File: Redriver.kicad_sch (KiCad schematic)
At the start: 124 parts, among them U1 DS320PR810NJXR, U2 DS320PR810NJXR

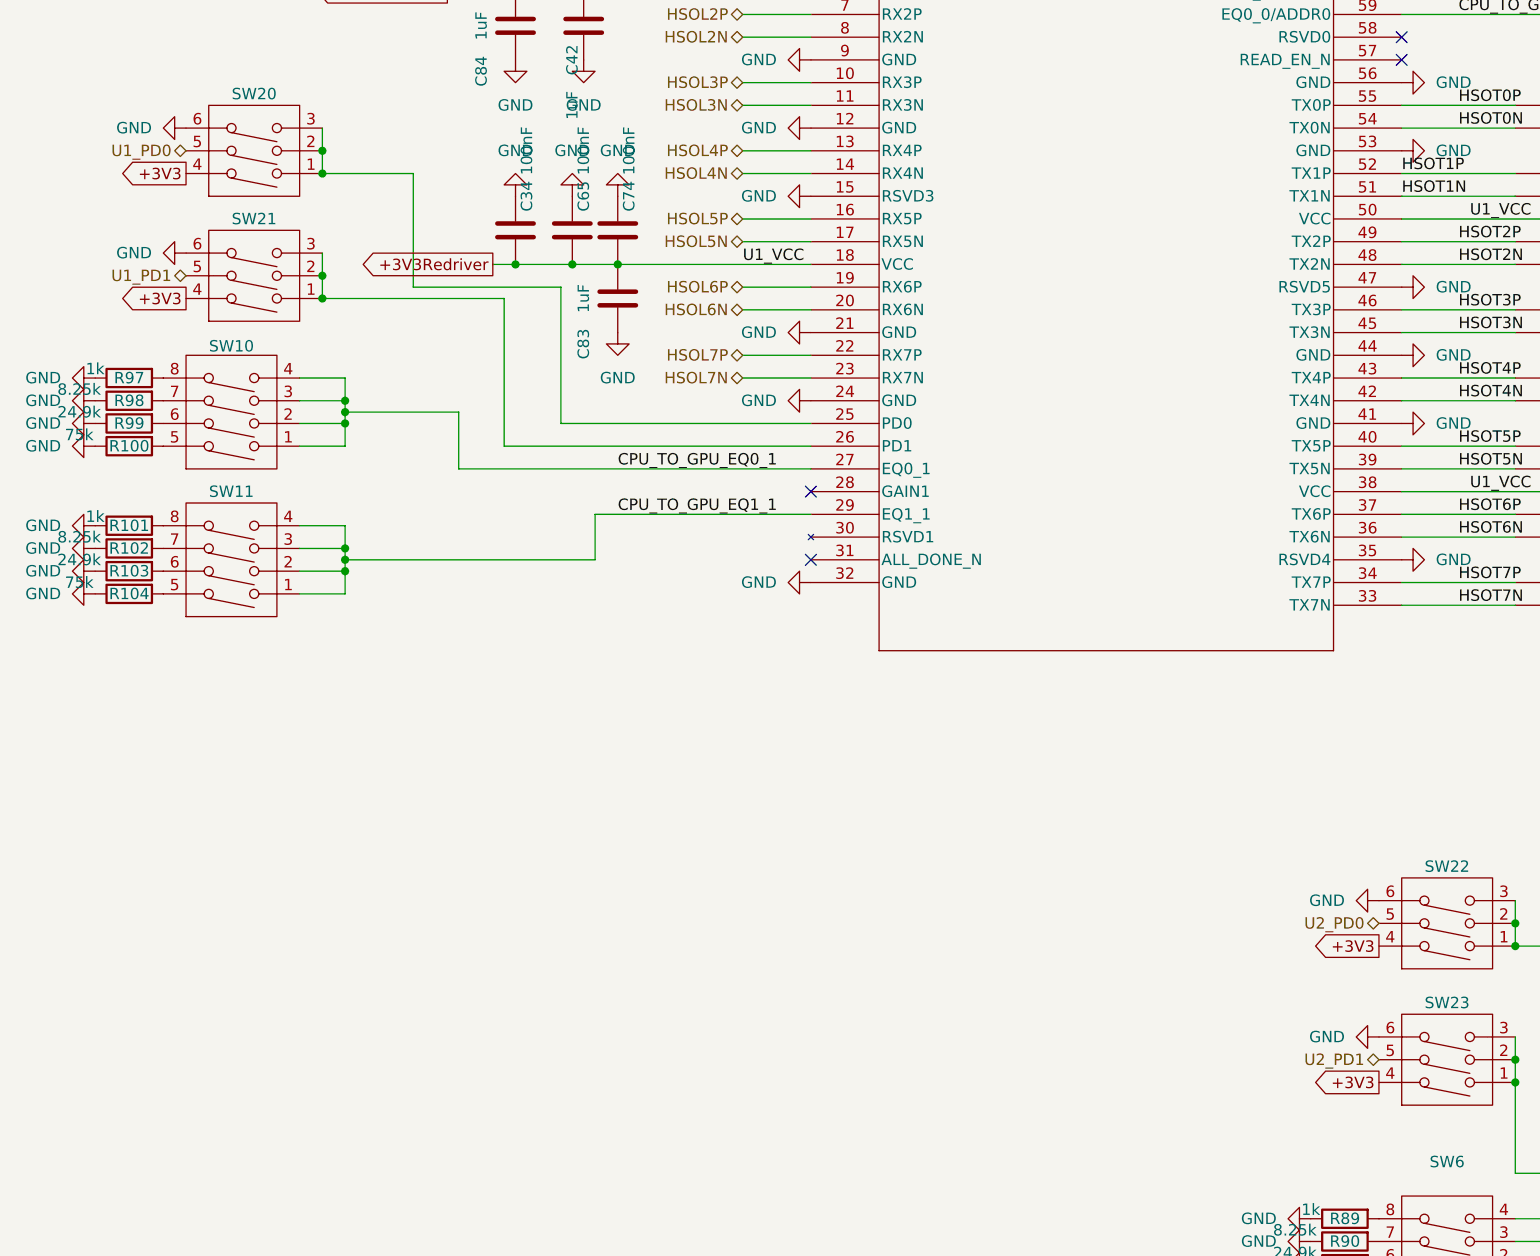
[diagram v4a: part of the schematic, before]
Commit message: added redrivers to proper 3.3v pd
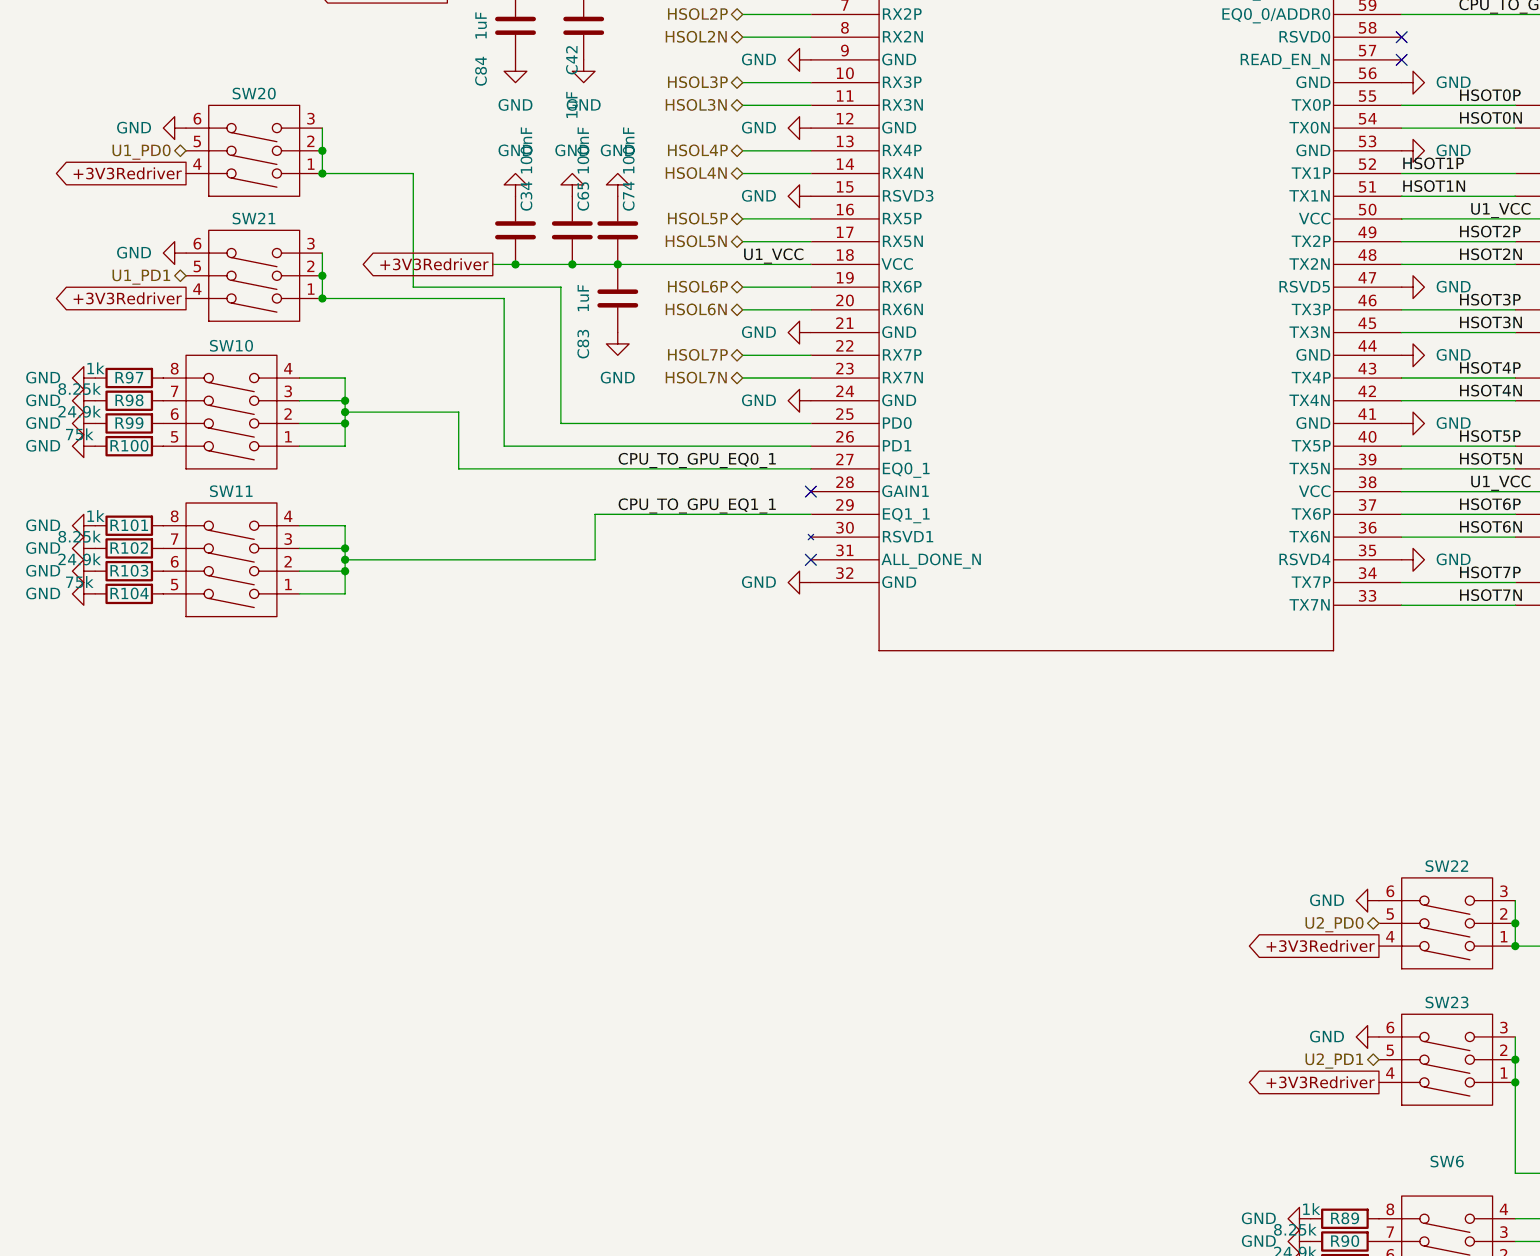
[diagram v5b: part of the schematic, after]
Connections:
- net +3V3 is gone; now on net +3V3Redriver: SW20.4, SW21.4, SW22.4, SW23.4
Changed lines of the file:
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@@
 		)
 	)
-	(global_label "+3V3"
+	(global_label "+3V3Redriver"
 		(shape output)
 		(at 123.19 104.14 180)
@@
 		)
 		(property "Intersheetrefs" "${INTERSHEET_REFS}"
-			(at 115.1248 104.14 0)
+			(at 107.3838 104.14 0)
 			(effects
 				(font
@@
 		)
 	)
-	(global_label "+3V3"
+	(global_label "+3V3Redriver"
 		(shape output)
 		(at -10.16 31.75 180)
@@
 		)
 		(property "Intersheetrefs" "${INTERSHEET_REFS}"
-			(at -18.2252 31.75 0)
+			(at -25.9662 31.75 0)
 			(effects
 				(font
@@
 		)
 	)
-	(global_label "+3V3"
+	(global_label "+3V3Redriver"
 		(shape output)
 		(at 123.19 119.38 180)
@@
 		)
 		(property "Intersheetrefs" "${INTERSHEET_REFS}"
-			(at 115.1248 119.38 0)
+			(at 107.3838 119.38 0)
 			(effects
 				(font
@@
 		)
 	)
-	(global_label "+3V3"
+	(global_label "+3V3Redriver"
 		(shape output)
 		(at -10.16 17.78 180)
@@
 		)
 		(property "Intersheetrefs" "${INTERSHEET_REFS}"
-			(at -18.2252 17.78 0)
+			(at -25.9662 17.78 0)
 			(effects
 				(font

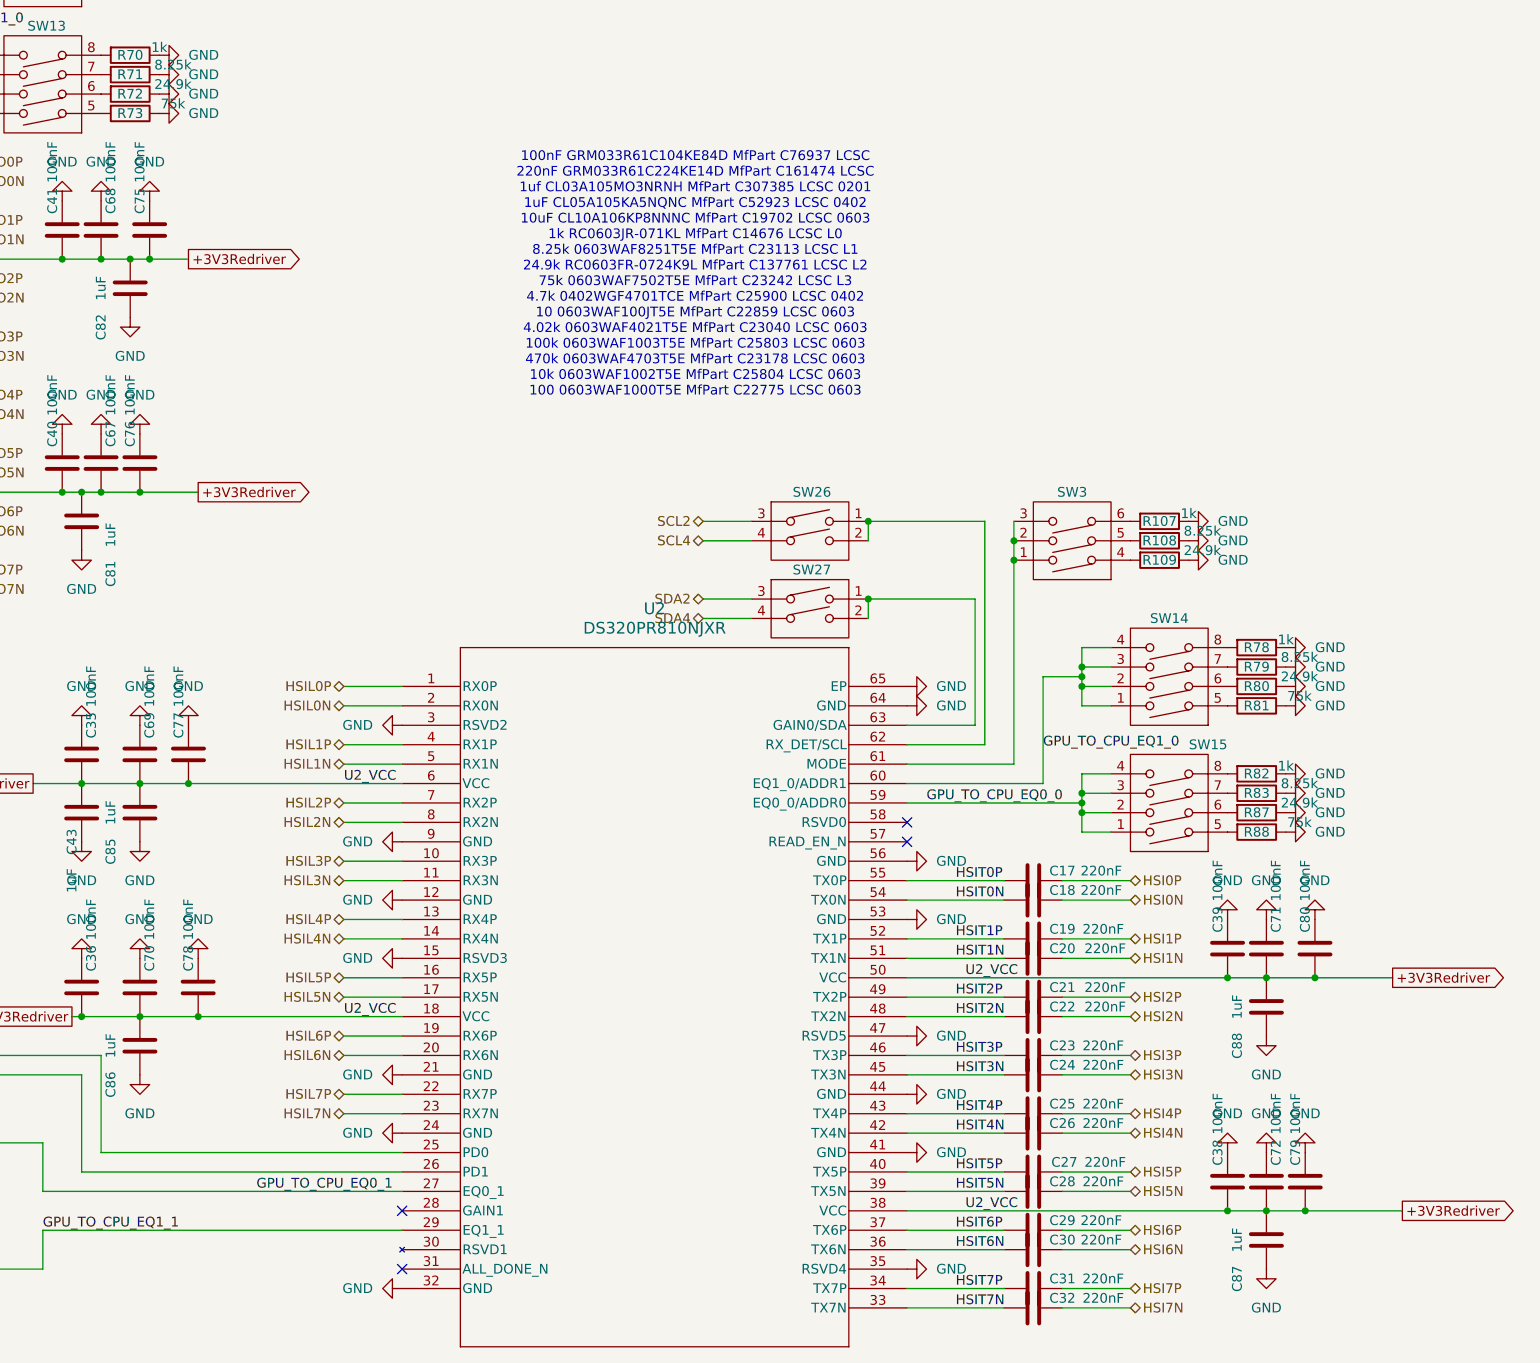
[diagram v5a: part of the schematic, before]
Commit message: added another set of decoupling caps for redriver rails
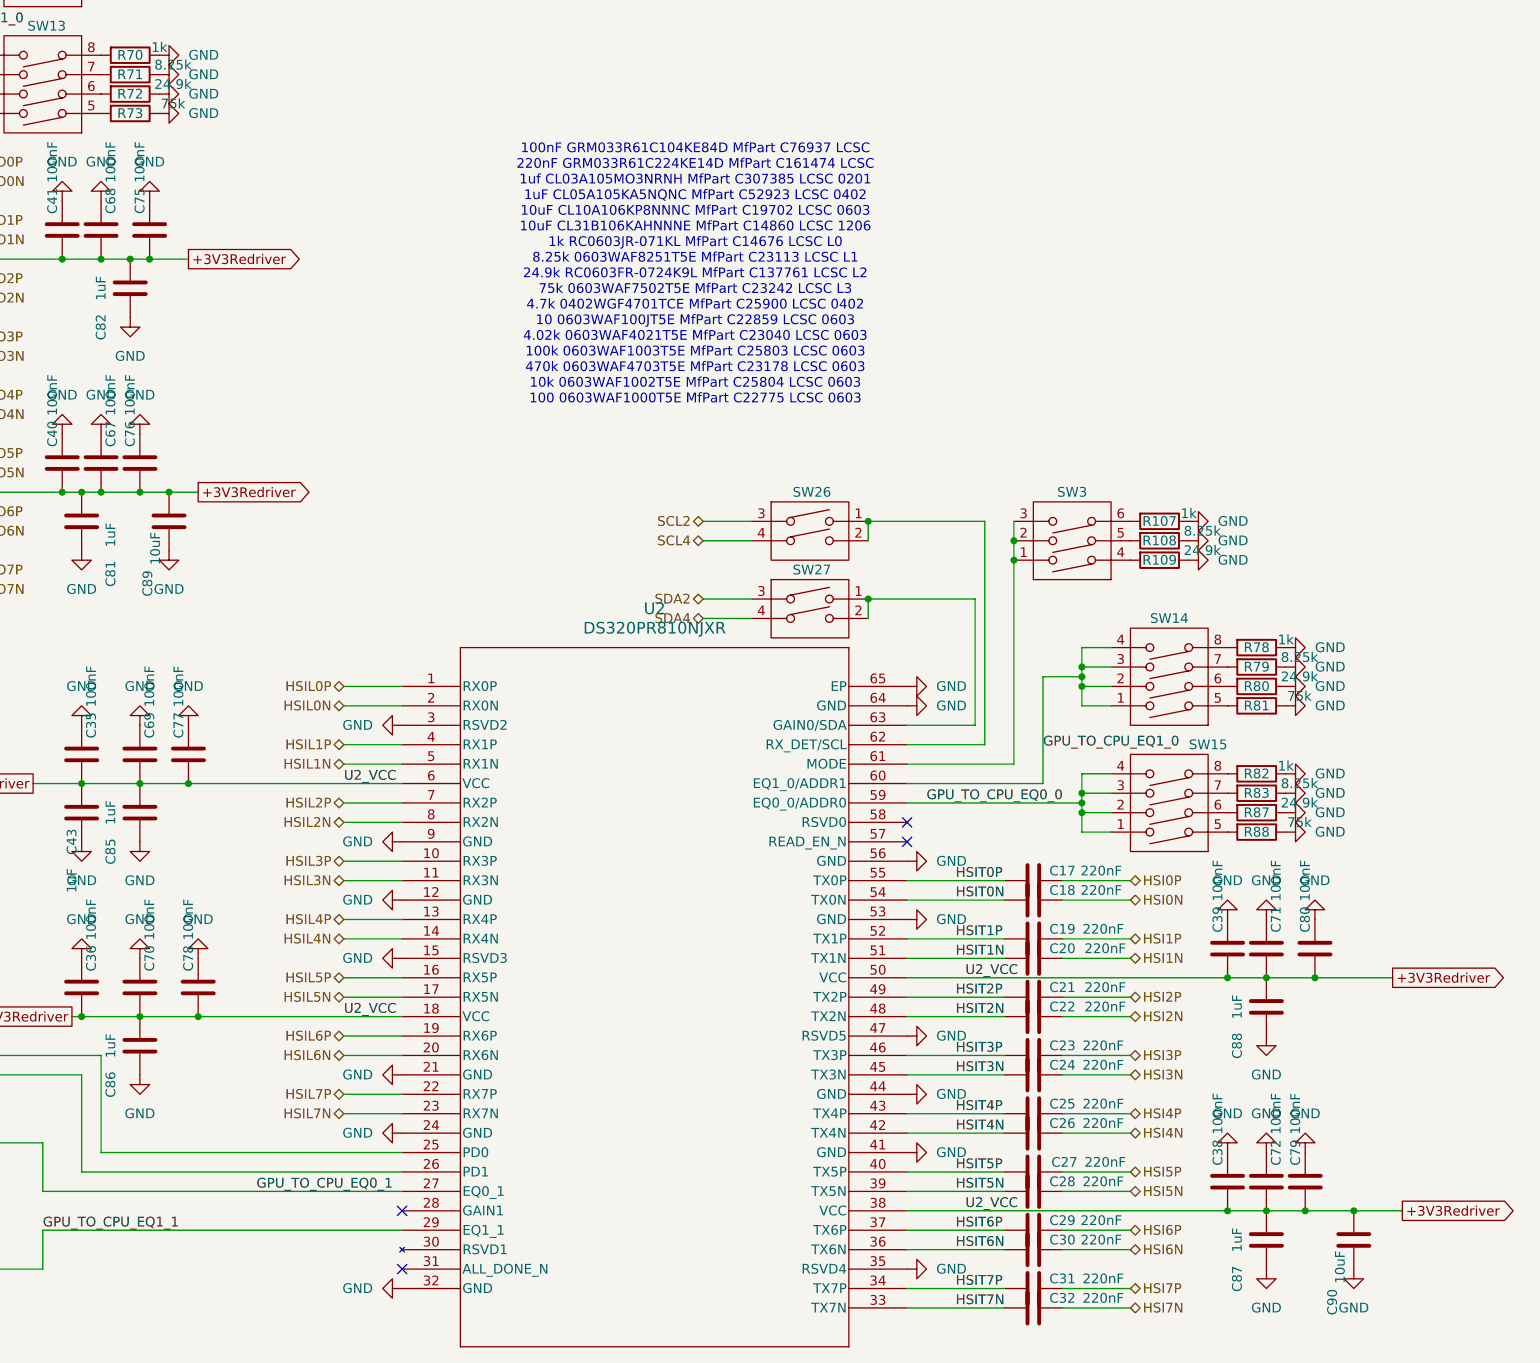
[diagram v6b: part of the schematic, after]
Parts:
- added C89, C90: 10uF, Capacitor_SMD:C_1206_3216Metric, symbol Device:C
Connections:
- net +3V3Redriver: now also C89.2, C90.2
- net GND: now also C89.1, C90.1
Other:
- note added: "100nF GRM033R61C104KE84D MfPart C76937 LCSC 220nF GRM033R61C224KE14D MfPart C161474 LCSC 1uf CL03A105MO3NRNH MfPart C307385 LCSC 0201 1uF CL05A105KA5NQNC MfPart C52923 LCSC 0402 10uF CL10A106KP8NNNC MfPart C19702 LCSC 0603 10uF CL31B106KAHNNNE MfPart C14860 LCSC 1206 1k RC0603JR-071KL MfPart C14676 LCSC L0 8.25k 0603WAF8251T5E MfPart C23113 LCSC L1 24.9k RC0603FR-0724K9L MfPart C137761 LCSC L2 75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"
- note removed: "100nF GRM033R61C104KE84D MfPart C76937 LCSC 220nF GRM033R61C224KE14D MfPart C161474 LCSC 1uf CL03A105MO3NRNH MfPart C307385 LCSC 0201 1uF CL05A105KA5NQNC MfPart C52923 LCSC 0402 10uF CL10A106KP8NNNC MfPart C19702 LCSC 0603 1k RC0603JR-071KL MfPart C14676 LCSC L0 8.25k 0603WAF8251T5E MfPart C23113 LCSC L1 24.9k RC0603FR-0724K9L MfPart C137761 LCSC L2 75k 0603WAF7502T5E MfPart C23242 LCSC L3 4.7k 0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"
